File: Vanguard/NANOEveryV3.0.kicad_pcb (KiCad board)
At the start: 2 copper layers, 14 parts, among them U1 ATMEGA4809, U2 AP2112K-3.3, U3 ATSAMD11D14A

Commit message: Start of layout
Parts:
- added D+0: DNP, TestPoint:TestPoint_THTPad_1.0x1.0mm_Drill0.5mm, F.Cu at (110.5, 28.9)
- added D-0: DNP, TestPoint:TestPoint_THTPad_1.0x1.0mm_Drill0.5mm, F.Cu at (110.5, 32.0)
- added D1: PRTR5V, Diode_SMD:D_SOD-323, F.Cu at (122.6, 45.7)
- added D2: PMEG6020, Diode_SMD:D_SOD-123, F.Cu at (104.0, 100.0)
- added D3: DNP, TestPoint:TestPoint_THTPad_1.0x1.0mm_Drill0.5mm, F.Cu at (110.5, 25.9)
- added DL1: YELLOW, LED_SMD:LED_0603_1608Metric, F.Cu at (128.9, 19.3)
- added DL2: GREEN, LED_SMD:LED_0603_1608Metric, F.Cu at (128.9, 21.9)
- added DL3: YELLOW, LED_SMD:LED_0603_1608Metric, F.Cu at (128.9, 24.5)
- added DL4: YELLOW, LED_SMD:LED_0603_1608Metric, F.Cu at (128.9, 27.1)
- added FD1: DNP, TestPoint:TestPoint_THTPad_1.0x1.0mm_Drill0.5mm, F.Cu at (110.5, 35.0)
- added FD2: DNP, TestPoint:TestPoint_THTPad_1.0x1.0mm_Drill0.5mm, F.Cu at (110.5, 38.1)
- added IC1: MPM3610, Package_DFN_QFN:DFN-18-1EP_3x5mm_P0.5mm_EP1.66x4.4mm, F.Cu at (122.5, 101.0)
- added J1: -, Connector_USB:USB_Micro-AB_Molex_47590-0001, F.Cu at (114.3, 109.5)
- added J2: DNP, Connector_PinHeader_1.00mm:PinHeader_2x03_P1.00mm_Vertical, F.Cu at (98.0, 80.5)
- added J3: Micro_SD_Card_Det1, Connector_Card:microSD_HC_Molex_104031-0811, F.Cu at (100.5, 64.5)
- added PB1: PTS820, Button_Switch_SMD:SW_Tactile_SPST_NO_Straight_CK_PTS636Sx25SMTRLFS, F.Cu at (113.5, 97.0)
- added Q1: BSS138PS, Package_TO_SOT_SMD:SOT-363_SC-70-6, F.Cu at (113.0, 83.0)
- added Q2: BSS138PS, Package_TO_SOT_SMD:SOT-363_SC-70-6, F.Cu at (104.5, 77.0)
- added Q3: BSS138, Package_TO_SOT_SMD:SOT-23, F.Cu at (122.8, 42.0)
- added R1: 1M, Resistor_SMD:R_0402_1005Metric, F.Cu at (119.0, 70.5)
- added R10: 100k, Resistor_SMD:R_0402_1005Metric, F.Cu at (126.5, 103.0)
- added R11: 4k7, Resistor_SMD:R_0402_1005Metric, F.Cu at (97.0, 83.0)
- added R12: 330R, Resistor_SMD:R_0402_1005Metric, F.Cu at (129.0, 97.5)
- added R13: 330R, Resistor_SMD:R_0402_1005Metric, F.Cu at (128.0, 97.5)
- added R14: 4k7, Resistor_SMD:R_0402_1005Metric, F.Cu at (104.0, 81.0)
- added R15: 4k7, Resistor_SMD:R_0402_1005Metric, F.Cu at (128.8, 67.5)
- added R16: 4k7, Resistor_SMD:R_0402_1005Metric, F.Cu at (105.0, 81.0)
- added R17: 4k7, Resistor_SMD:R_0402_1005Metric, F.Cu at (128.8, 71.5)
- added R18: 4k7, Resistor_SMD:R_0402_1005Metric, F.Cu at (107.5, 81.0)
- added R19: 4k7, Resistor_SMD:R_0402_1005Metric, F.Cu at (109.0, 69.5)
- added R2: 330R, Resistor_SMD:R_0402_1005Metric, F.Cu at (116.0, 83.0)
- added R3: 330R, Resistor_SMD:R_0402_1005Metric, F.Cu at (117.5, 69.5)
- added R4: 100k, Resistor_SMD:R_0402_1005Metric, F.Cu at (119.0, 83.0)
- added R5: 4k7, Resistor_SMD:R_0402_1005Metric, F.Cu at (102.0, 79.0)
- added R6: 100k, Resistor_SMD:R_0402_1005Metric, F.Cu at (119.0, 91.5)
- added R7: 0R, Resistor_SMD:R_0402_1005Metric, F.Cu at (108.5, 81.0)
- added R8: 19k1, Resistor_SMD:R_0402_1005Metric, F.Cu at (119.0, 89.0)
- added R9: 39k, Resistor_SMD:R_0402_1005Metric, F.Cu at (125.0, 97.5)
- added U4: ICM-20602, Package_LGA:LGA-16_3x3mm_P0.5mm_LayoutBorder3x5y, F.Cu at (113.5, 89.0)
- moved C3 120.6 mm to (127.5, 107.0), turned to 90 degrees
- moved C11 120.0 mm to (126.5, 100.0), turned to 90 degrees
- moved C1 119.5 mm to (122.5, 107.0), turned to 90 degrees
- moved C8 118.9 mm to (122.5, 97.5), turned to -90 degrees
- moved C4 116.7 mm to (125.0, 107.0), turned to 90 degrees
- moved C9 116.1 mm to (120.5, 97.5), turned to -90 degrees
- moved C10 115.7 mm to (121.5, 97.5), turned to -90 degrees
- moved C5 113.3 mm to (119.0, 87.0)
- moved C2 112.7 mm to (119.0, 84.0), turned to 180 degrees
- moved C7 111.5 mm to (119.0, 88.0)
- moved C6 110.9 mm to (119.0, 85.0), turned to 180 degrees
- moved U2 107.9 mm to (129.0, 101.0), turned to 90 degrees
- moved U1 93.9 mm to (113.3, 74.8), turned to 45 degrees
- moved U3 84.4 mm to (102.5, 90.0), turned to 90 degrees
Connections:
- U1 pad 8: /TX0 -> /RX0
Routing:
- net GND: track 0.00 -> 77.0 mm, vias 0 -> 12
- net +5V: track 0.00 -> 63.6 mm, vias 0 -> 4
- net +3V3: track 0.00 -> 60.9 mm, vias 0 -> 3
- net VIN: track 0.00 -> 22.7 mm
- net Net-(C1-Pad1): track 0.00 -> 21.6 mm
- net /UPDI: track 0.00 -> 16.8 mm
- net Net-(IC1-FB): track 0.00 -> 15.6 mm
- net /RX0: track 0.00 -> 11.0 mm
- net Net-(U3A-PA28/RESETN): track 0.00 -> 8.91 mm
- net Net-(U3A-PA30/SWCLK): track 0.00 -> 7.45 mm
- net Net-(U3A-PA31/SWDIO): track 0.00 -> 7.00 mm
- net Net-(IC1-AAM): track 0.00 -> 4.81 mm
- net /RX_D11: track 0.00 -> 4.69 mm
- net /TX_D11: track 0.00 -> 4.58 mm
- net Net-(IC1-EN): track 0.00 -> 3.70 mm
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- added copper zone on B.Cu, net (none)
- added copper zone on In2.Cu, net +5V
- added copper zone on In1.Cu, net GND
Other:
- board outline added: 40 x 55 mm
- copper layers 2 -> 4

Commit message: some more layout shenangins
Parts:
- added C12: 2.2uF, Capacitor_SMD:C_0402_1005Metric, F.Cu at (116.5, 91.0)
- added C13: 0.1uF, Capacitor_SMD:C_0402_1005Metric, F.Cu at (116.5, 90.0)
- added R20: DNP, Resistor_SMD:R_0402_1005Metric, F.Cu at (100.5, 77.5)
- added R21: 538Ω, Resistor_SMD:R_0402_1005Metric, F.Cu at (116.5, 87.0)
- added R22: 645Ω, Resistor_SMD:R_0402_1005Metric, F.Cu at (116.5, 88.0)
- moved D1 56.5 mm to (113.5, 101.5)
- moved R1 33.9 mm to (113.5, 104.0), turned to 90 degrees
- moved Q3 25.5 mm to (114.0, 66.0), turned to 90 degrees
- moved R15 20.8 mm to (113.0, 81.0)
- moved D2 17.6 mm to (87.5, 106.0)
- moved R17 16.3 mm to (116.0, 81.5)
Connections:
- C3 pad 1: +5V -> Net-(U2-EN)
- C4 pad 1: VIN -> Net-(IC1-VIN)
- IC1 pad 16: VIN -> Net-(IC1-VIN)
- IC1 pad 7: +5V -> Net-(U2-EN)
- IC1 pad 8: +5V -> Net-(U2-EN)
- IC1 pad 9: +5V -> Net-(U2-EN)
- J1 pad 1: VIN -> Net-(D1-Pad4)
- R10 pad 2: VIN -> Net-(IC1-VIN)
- R6 pad 2: +5V -> Net-(U2-EN)
- U1 pad 35: unconnected-(U1-PF01-Pad35) -> 1.8V temp scl
- U1 pad 36: /A4/SDA -> 1.8v temp sda
- U1 pad 46: /A4/SDA -> 1.8v temp sda
- U2 pad 1: +5V -> Net-(U2-EN)
- U2 pad 3: +5V -> Net-(U2-EN)
- U4 pad 16: unconnected-(U4-VDD-Pad16) -> Net-(U4-VDD)
- U4 pad 2: unconnected-(U4-SCL/SPC-Pad2) -> /D9~{}
- U4 pad 3: /RX0 -> 1.8v temp sda
- U4 pad 5: +3.3V -> unconnected-(U4-~{CS}-Pad5)
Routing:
- net VIN: track 22.7 -> 0.00 mm
- net Net-(IC1-VIN): track 0.00 -> 22.7 mm
- net /TX_UPDI: track 1.00 -> 17.4 mm
- net /AREF: track 1.00 -> 17.1 mm
- net /TX_D11: track 4.58 -> 18.5 mm, vias 0 -> 2
- net /RESETN: track 1.02 -> 10.7 mm, vias 0 -> 1
- net +3V3: track 60.9 -> 70.2 mm, vias 3 -> 4
- net GND: track 77.0 -> 84.1 mm, vias 12 -> 13
- net +5V: track 63.6 -> 70.1 mm
- net Net-(C1-Pad1): track 21.6 -> 27.8 mm
- net Net-(U4-VDD): track 0.00 -> 5.77 mm
- net /USB_P: track 0.00 -> 5.44 mm
- net /RX0: track 11.0 -> 16.4 mm
- net /RX_UPDI: track 0.00 -> 4.45 mm
- net /A4/SDA: track 0.00 -> 3.47 mm
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- added copper zone on In3.Cu, net (none)
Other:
- copper layers 4 -> 6

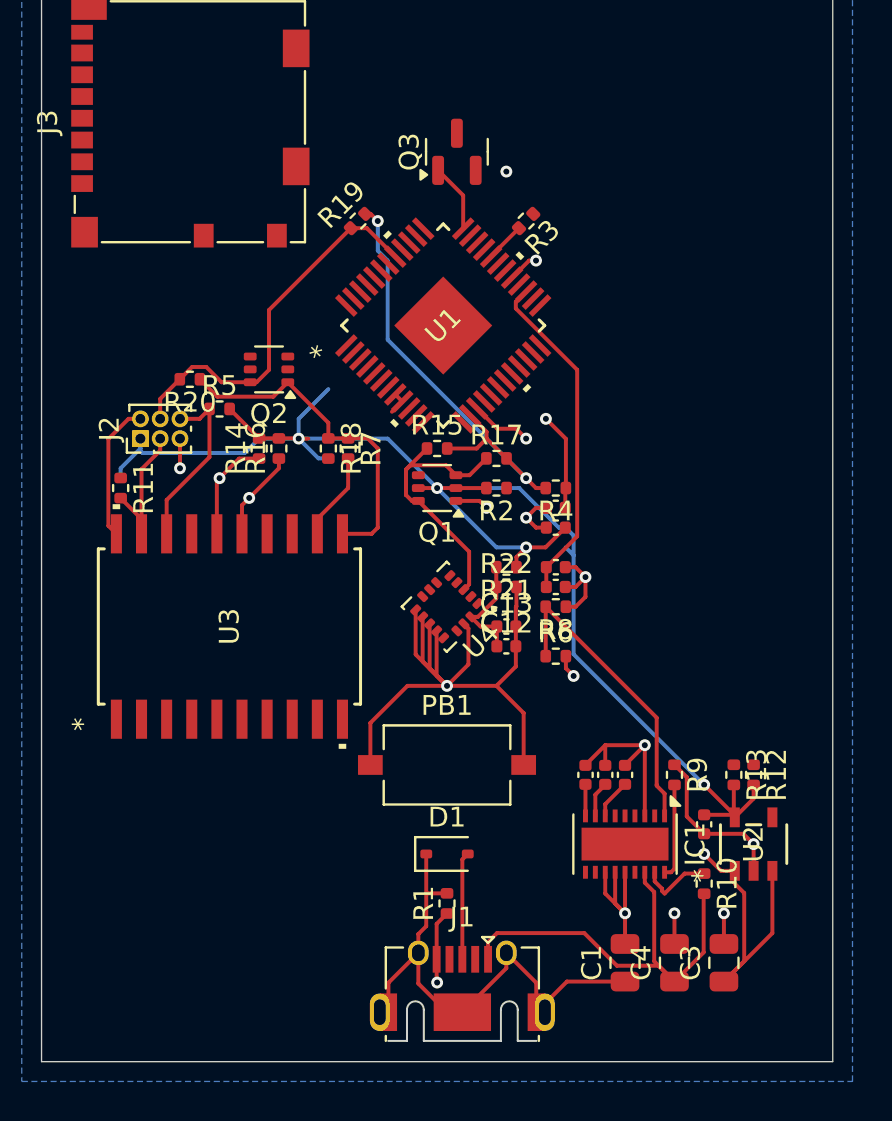
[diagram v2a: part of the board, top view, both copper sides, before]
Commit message: finished layout except sd card
lots of discontinuities need to be fixed
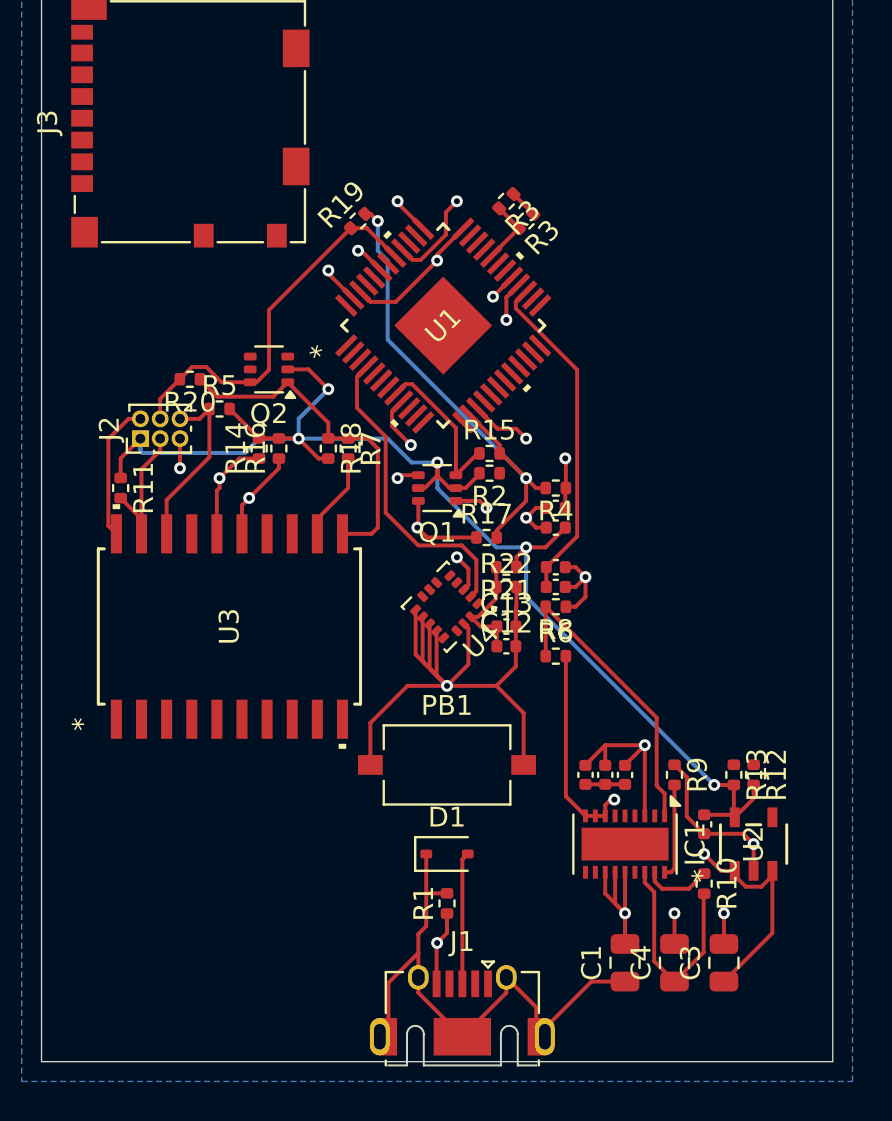
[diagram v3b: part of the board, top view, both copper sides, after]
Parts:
- removed Q3: BSS138, Package_TO_SOT_SMD:SOT-23
- added R3: 330R, Resistor_SMD:R_0402_1005Metric, F.Cu at (116.5, 68.5)
- C12: value 2.2uF -> 4u7
- C13: value 0.1uF -> 0u1
- moved R17 4.03 mm to (115.5, 85.5)
- moved R15 2.66 mm to (115.7, 81.2)
- moved J1 1.24 mm to (114.3, 110.7)
- moved R2 0.83 mm to (115.7, 82.2)
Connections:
- Q1 pad 3: /RX0 -> /TX0
- R15 pad 1: /RX0 -> /TX0
- U1 pad 8: /RX0 -> /TX0
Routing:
- net Net-(U2-EN): track 0.00 -> 27.7 mm, vias 0 -> 2
- net 1.8v temp sda: track 0.00 -> 24.9 mm, vias 0 -> 2
- net /D9~{}: track 0.00 -> 15.8 mm
- net +5V: track 70.1 -> 55.3 mm, vias 4 -> 3
- net /RESETN: track 10.7 -> 22.7 mm, vias 1 -> 2
- net Net-(IC1-VIN): track 22.7 -> 11.2 mm
- net /RX_D11: track 5.28 -> 15.4 mm, vias 1 -> 2
- net /A5/SCL: track 0.00 -> 9.31 mm, vias 0 -> 2
- net /TX0: track 0.00 -> 8.24 mm
- net /RX0: track 16.4 -> 11.7 mm, vias 0 -> 2
- net /A4/SDA: track 3.47 -> 0.00 mm
- net Net-(C1-Pad1): track 27.8 -> 29.7 mm
- net GND: track 84.1 -> 85.6 mm
- net +3V3: track 70.2 -> 68.8 mm, vias 4 -> 5
- net /SCK: track 2.02 -> 3.43 mm
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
